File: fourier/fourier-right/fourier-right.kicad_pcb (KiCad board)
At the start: 2 copper layers, 129.2 x 80.4 mm, 145 parts, among them J1 VCC, J3 RGB, J6 C6, J7 GND, U1 ProMicro, U2 TRRS

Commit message: face controller forward and move LED breakout ports to unifrom position
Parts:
- removed G***: LOGO, Keebio-Art:Keebio-TwoTone
- removed G***: LOGO, Keebio-Art:AIRI-Logo2
- removed G***: LOGO, Keebio-Art:Fourier-Rect
- removed G***: LOGO, Keebio-Art:Fourier-1.2
- moved J1 103.2 mm to (53.2, 56.7)
- moved J3 103.2 mm to (53.2, 60.9)
- moved J7 103.2 mm to (53.2, 65.0)
- moved U1 71.8 mm to (71.3, 30.1), turned to 270 degrees
- moved D_A2 19.0 mm to (60.8, 33.3)
- moved SW_RST1 4.43 mm to (54.2, 15.9)
- moved U2 4.43 mm to (43.4, 13.3)
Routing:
- net reset: track 132.4 -> 27.9 mm, vias 2 -> 0
- net C6: track 3.24 -> 79.6 mm, vias 0 -> 1
- net GND: track 183.1 -> 110.1 mm, vias 3 -> 10
- net data2: track 123.2 -> 51.1 mm
- net col7: track 130.7 -> 199.3 mm, vias 0 -> 1
- net data: track 120.5 -> 52.2 mm, vias 1 -> 0
- net VCC: track 160.3 -> 93.7 mm, vias 3 -> 1
- net col3: track 109.2 -> 55.2 mm, vias 3 -> 0
- net col2: track 158.8 -> 106.4 mm, vias 2 -> 1
- net col1: track 180.0 -> 133.1 mm
- net col6: track 74.9 -> 116.9 mm, vias 0 -> 1
- net Net-(D_A2-Pad2): track 33.6 -> 6.16 mm
- net rowA: track 136.8 -> 112.0 mm
- net rowB: track 119.1 -> 142.3 mm
- net RGB: track 35.8 -> 57.4 mm
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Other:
- board size 129.2 x 80.4 mm -> 129.2 x 85.2 mm
- board text added: "Fourier 1.3"

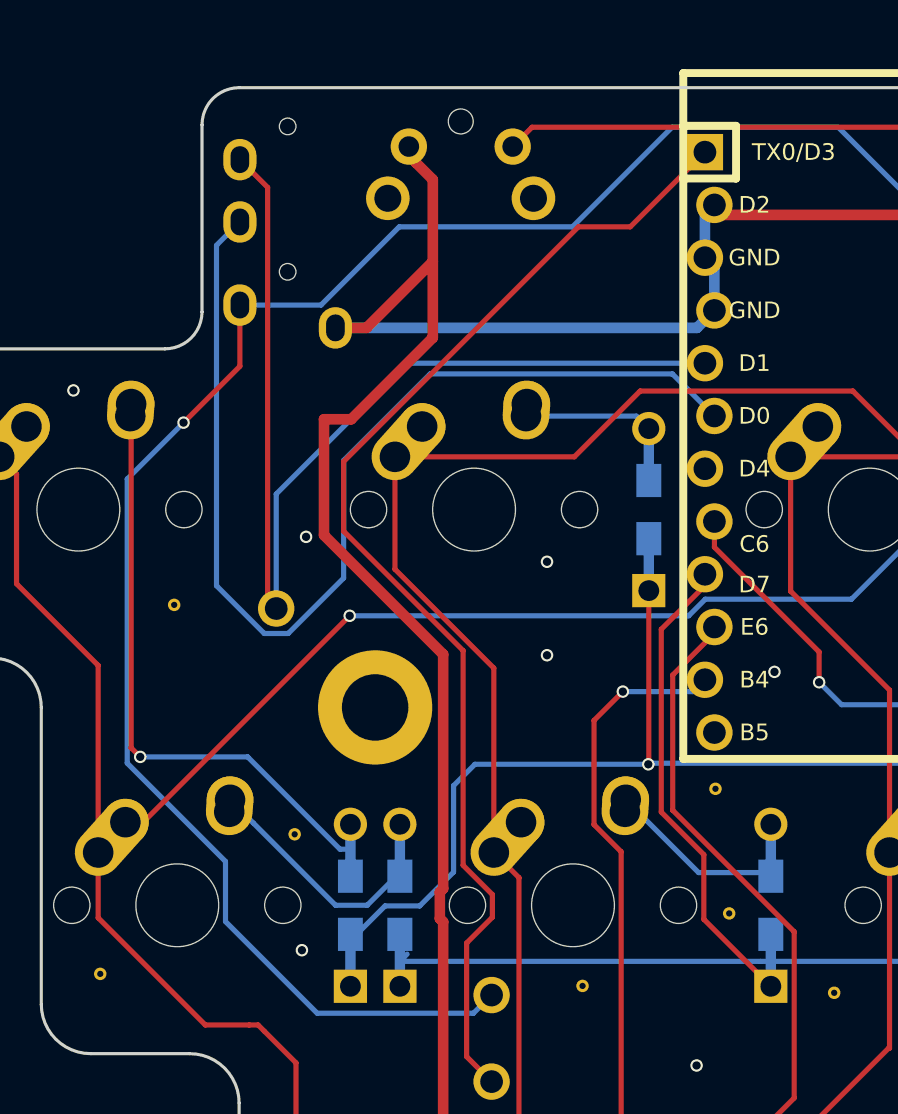
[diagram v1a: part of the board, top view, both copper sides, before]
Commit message: fixed connections and ran DRC
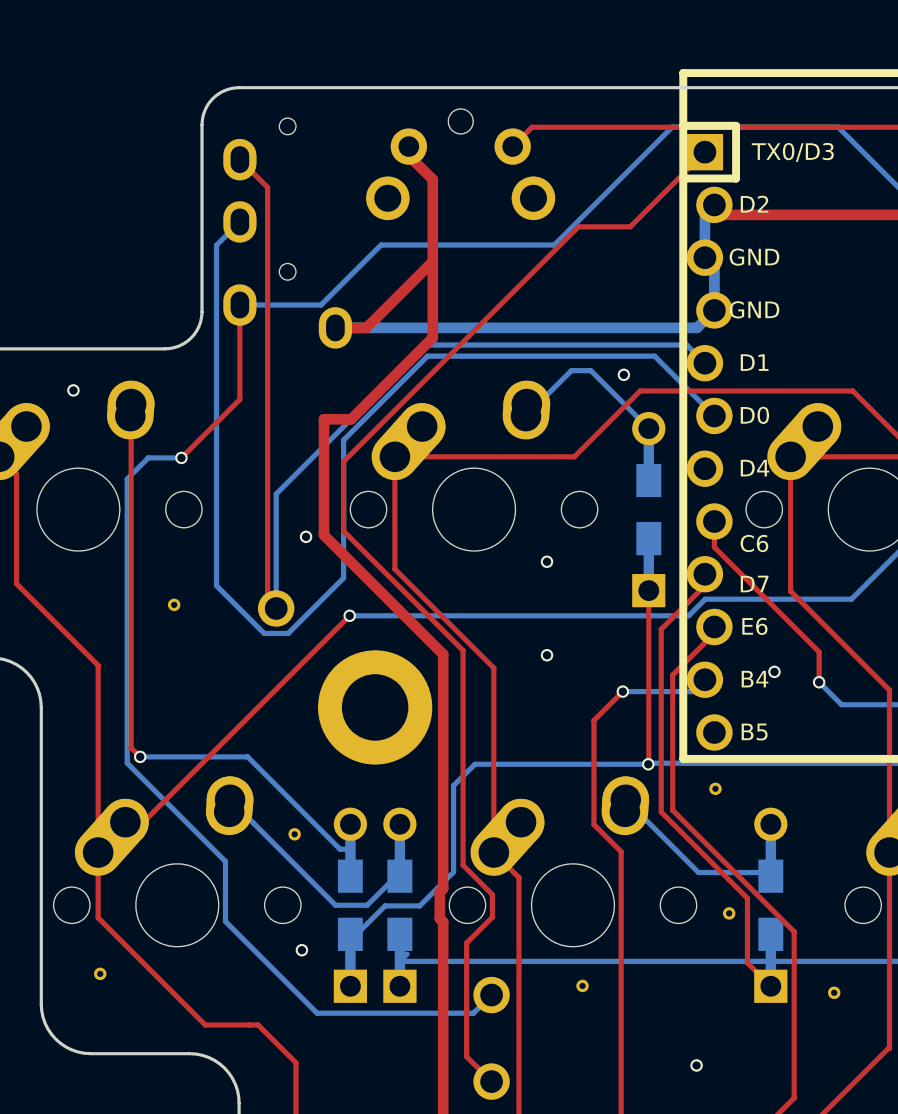
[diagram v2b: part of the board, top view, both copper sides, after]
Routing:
- net Net-(D_A2-Pad2): track 6.16 -> 7.97 mm
- net data: track 52.2 -> 53.5 mm
- net VCC: track 93.7 -> 94.7 mm
- net data2: track 51.1 -> 51.8 mm
- net GND: vias 10 -> 11

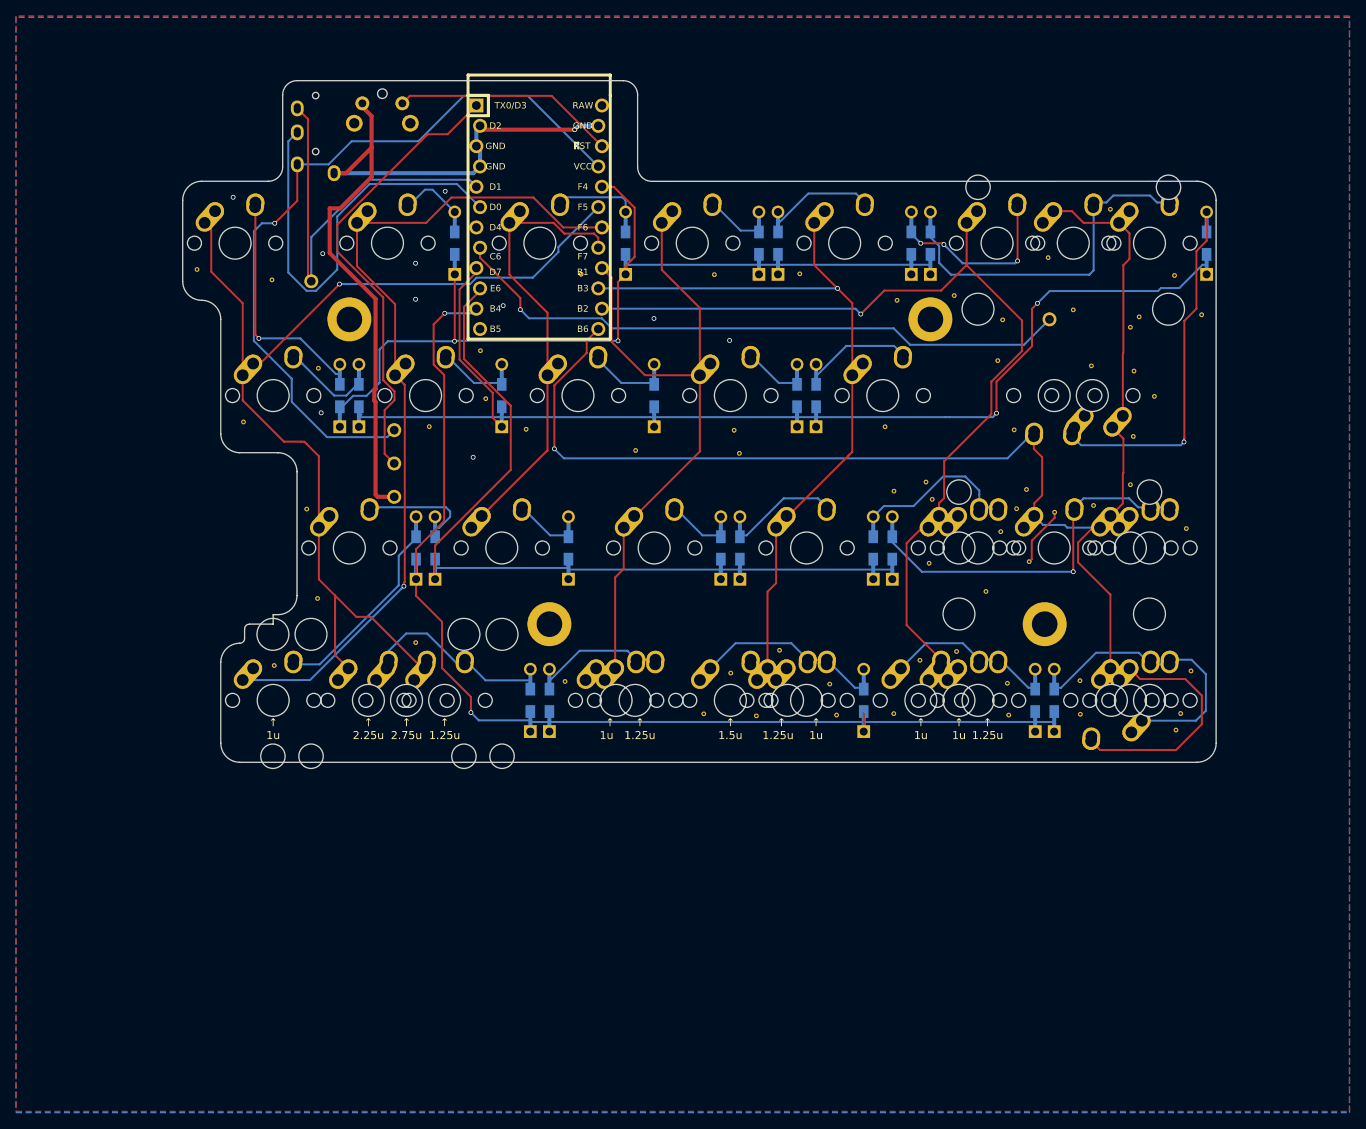
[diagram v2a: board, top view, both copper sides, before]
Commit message: rotate right top to correct orientation and upgraded to KiCad 5.99
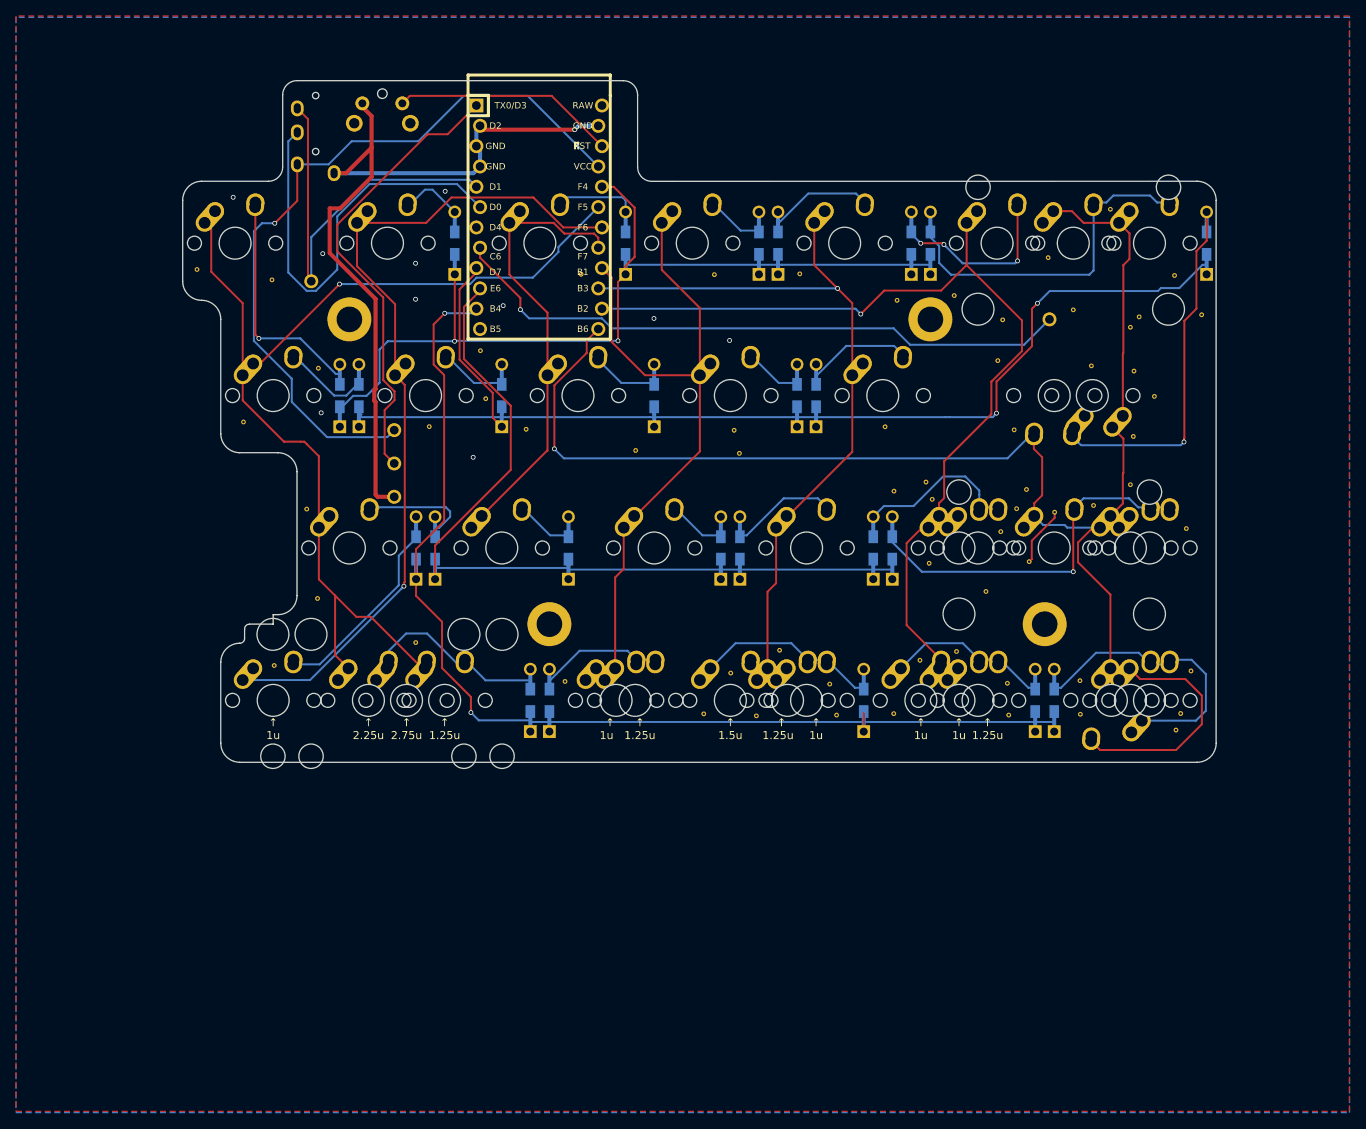
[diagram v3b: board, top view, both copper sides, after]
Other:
- net class Default removed
- net class Power removed
